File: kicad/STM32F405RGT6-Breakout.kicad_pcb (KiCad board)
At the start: 4 copper layers, 71.9 x 57 mm, 57 parts, among them J1 USB_C_Receptacle_USB2.0, J2 Uno Power, J3 SWD/JTAG, J4 Uno Analog, J5 Uno Digital 2, J6 Uno Digital 1, Q1 Si2301CDS, SW1 TS-1187A-B-A-B, SW2 TS-1187A-B-A-B, U1 STM32F405RGT6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

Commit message: Revert "First ever attempt at actual routing, it went terribly"
This reverts commit ef1419a7460263513f620155a18387d495a8f3db.

lol
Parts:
- moved R7 105.0 mm to (210.4, 137.8), turned to 0 degrees
- moved R8 76.7 mm to (207.0, 133.4), turned to 0 degrees
- moved R3 59.8 mm to (197.0, 144.4), turned to 0 degrees
- moved R4 57.5 mm to (195.0, 144.4), turned to 0 degrees
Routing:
- net NRST: track 105.5 -> 7.55 mm, vias 6 -> 0
- net I2C1_SDA: track 93.6 -> 0.00 mm, vias 3 -> 0
- net I2C1_SCL: track 90.9 -> 0.00 mm, vias 3 -> 0
- net USART6_RX: track 53.7 -> 0.00 mm, vias 2 -> 0
- net SWO: track 52.6 -> 0.00 mm, vias 2 -> 0
- net USART6_TX: track 46.4 -> 0.00 mm, vias 2 -> 0
- net BOOT0: track 46.0 -> 0.00 mm, vias 2 -> 0
- net +3.3VA: track 48.6 -> 4.44 mm, vias 2 -> 0
- net SWDIO: track 41.8 -> 0.00 mm, vias 2 -> 0
- net GPIO_PA0: track 41.0 -> 0.00 mm, vias 2 -> 0
- net SWCLK: track 40.1 -> 0.00 mm, vias 2 -> 0
- net GPIO_PA2: track 37.5 -> 0.00 mm
- net SPI1_MISO: track 33.2 -> 0.00 mm, vias 2 -> 0
- net GPIO_PA1: track 32.3 -> 0.00 mm, vias 2 -> 0
- net GPIO_PA3: track 31.6 -> 0.00 mm, vias 3 -> 0
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
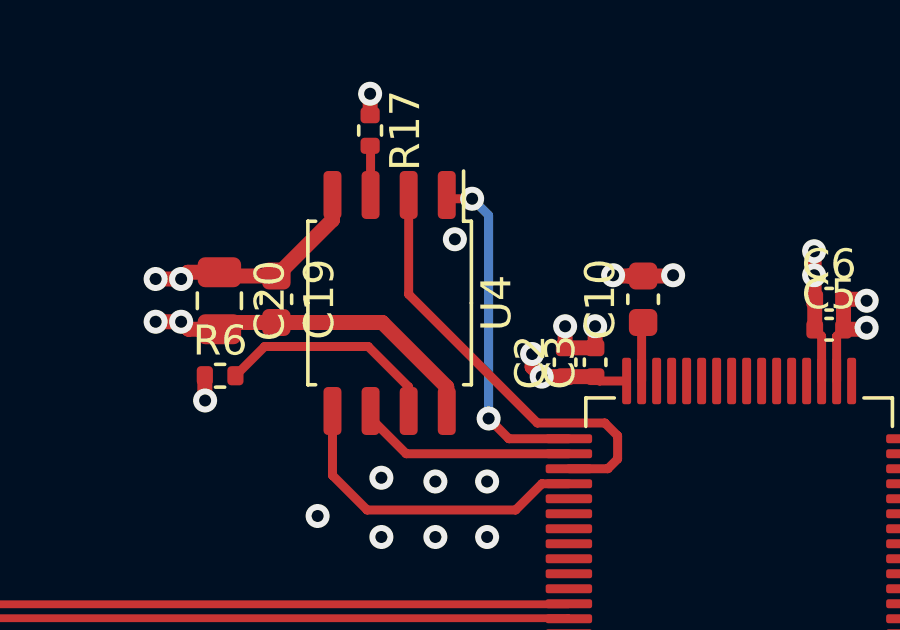
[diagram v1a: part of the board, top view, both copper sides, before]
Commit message: run the SPI flash CS a little shorter on the bottom
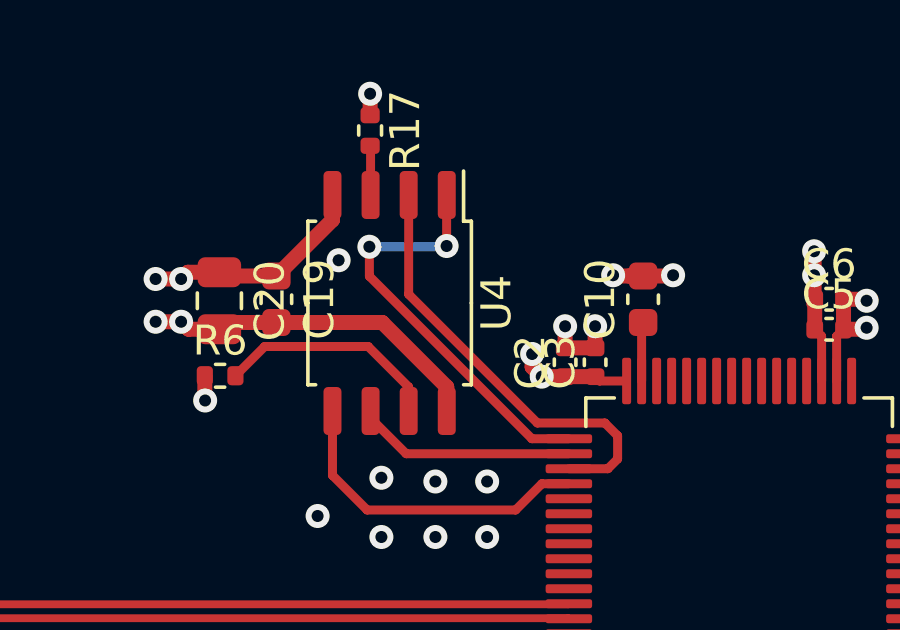
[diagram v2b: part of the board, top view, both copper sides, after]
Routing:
- net FLASH_CS: track 11.4 -> 14.3 mm
